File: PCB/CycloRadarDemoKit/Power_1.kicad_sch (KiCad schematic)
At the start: 33 parts, among them J701 20-16V Supply Voltage, Q701 SI2309CDS, U701 INA3221, U702 RT8259, U703 AP63205WU

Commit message: USB layout, long traces from upper prepaired
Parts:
- R710, R713: LCSC C22764 -> C22975
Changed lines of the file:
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@@
       (effects (font (size 1.27 1.27)) hide)
     )
-    (property "LCSC" "C22764" (at 212.725 127 0)
+    (property "LCSC" "C22975" (at 212.725 127 0)
       (effects (font (size 1.27 1.27)) hide)
     )
@@
       (effects (font (size 1.27 1.27)) hide)
     )
-    (property "LCSC" "C22764" (at 140.97 175.26 0)
-      (effects (font (size 1.27 1.27)) hide)
-    )
+    (property "LCSC" "C22975" (at 140.97 175.26 0)
+      (effects (font (size 1.27 1.27)) hide)
+    )

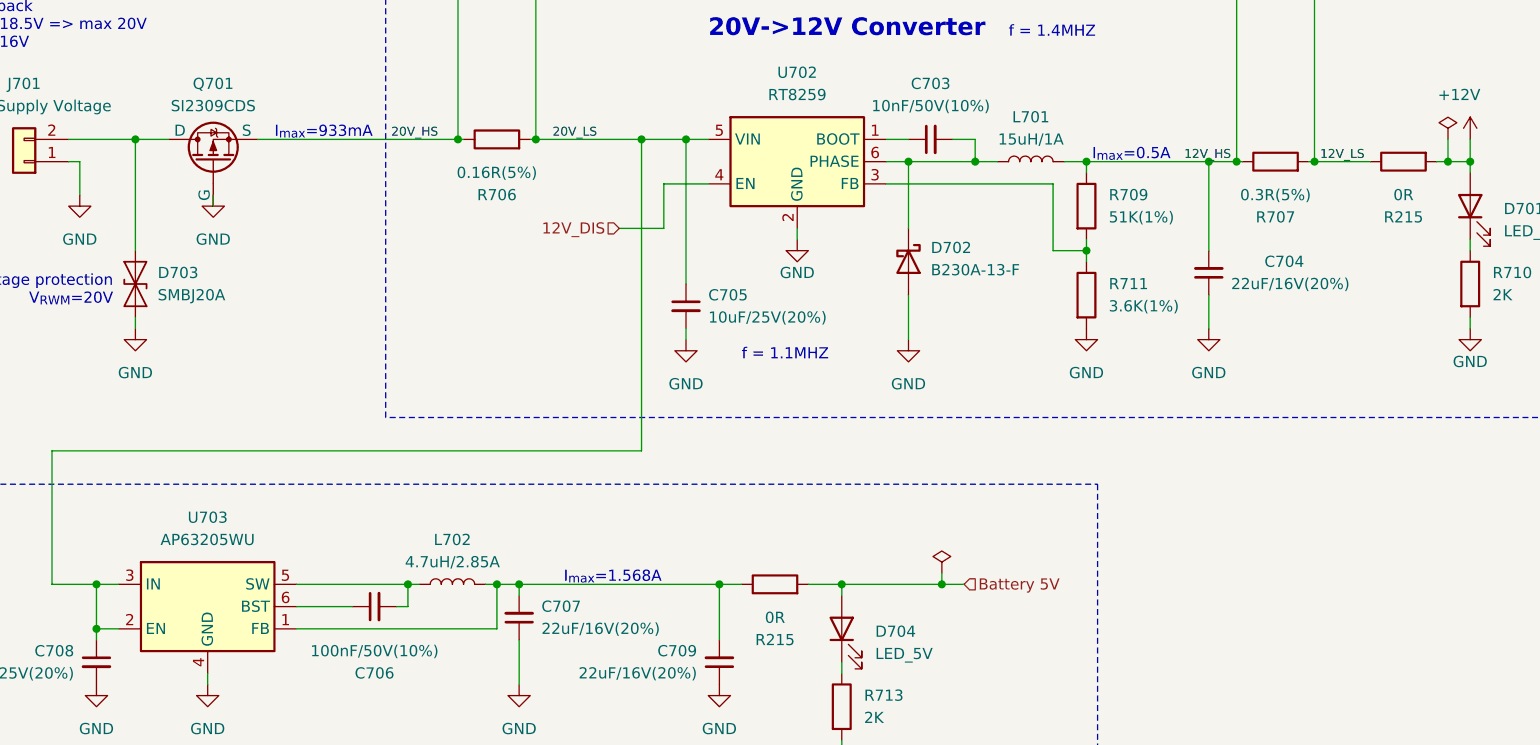
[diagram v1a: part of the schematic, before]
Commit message: DC/DC routed, stuckup properties changed
ready for PCB resize
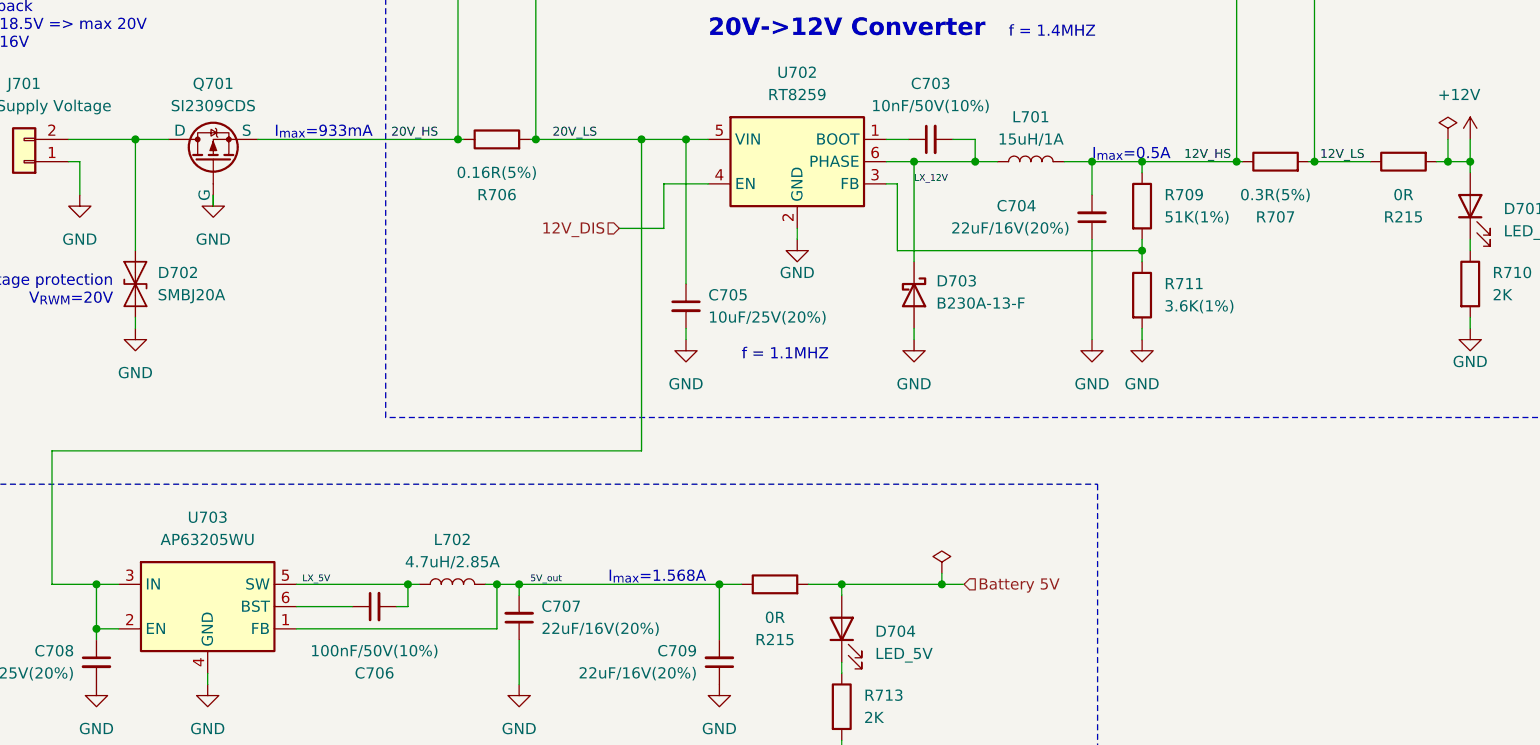
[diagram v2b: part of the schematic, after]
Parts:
- C705, C708: footprint Capacitor_SMD:C_0603_1608Metric -> Capacitor_SMD:C_1206_3216Metric; LCSC C96446 -> C13585
- renumbered D703 to D702, D702 to D703
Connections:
- net 5V_out: now reaches C707.2, C709.2, L702.2, R215.1, U703.1 (FB)
- net LX_12V: now reaches C703.2, D703.1 (K), L701.1, U702.6 (PHASE)
- net LX_5V: now reaches C706.2, L702.1, U703.5 (SW)
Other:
- moved on the sheet: C704, D703, R709, R711

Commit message: PCB routing done
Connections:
- net IN_20V: now reaches D702.2 (A2), J701.2 (Pin_2), Q701.1 (D)
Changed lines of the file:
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@@
     (effects (font (size 1.016 1.016)) (justify left bottom))
+  )
+  (label "IN_20V" (at 55.245 110.49 0) (fields_autoplaced)
+    (effects (font (size 0.762 0.762)) (justify left bottom))
   )
   (label "12V_HS" (at 185.42 113.03 180) (fields_autoplaced)

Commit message: start of repair after review
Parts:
- C705, C708: value 10uF/25V(20%) -> 10uF/50V(20%)
- R706: value 0.16R(5%) -> 0.18R(5%); footprint Resistor_SMD:R_1210_3225Metric -> Resistor_SMD:R_Shunt_LTR10EVHJLR18; LCSC C175910 -> C253348
- R707: LCSC C175910 -> C188102
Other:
- note added: "I_{max}=1.28A"
- note added: "I_{max}=842mA"
- note removed: "I_{max}=1.568A"
- note removed: "I_{max}=933mA"
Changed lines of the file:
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@@
     (effects (font (size 1.27 1.27)) (justify left bottom))
   )
-  (text "I_{max}=933mA" (at 76.2 110.49 0)
+  (text "I_{max}=842mA" (at 76.2 110.49 0)
     (effects (font (size 1.27 1.27)) (justify left bottom))
   )
@@
     (effects (font (size 1.27 1.27)) (justify left bottom))
   )
-  (text "I_{max}=1.568A" (at 114.3 161.29 0)
+  (text "I_{max}=1.28A" (at 114.3 161.29 0)
     (effects (font (size 1.27 1.27)) (justify left bottom))
   )
@@
       (effects (font (size 1.27 1.27)))
     )
-    (property "Value" "0.16R(5%)" (at 101.6 114.3 90)
-      (effects (font (size 1.27 1.27)))
-    )
-    (property "Footprint" "Resistor_SMD:R_1210_3225Metric" (at 101.6 112.268 90)
+    (property "Value" "0.18R(5%)" (at 101.6 114.3 90)
+      (effects (font (size 1.27 1.27)))
+    )
+    (property "Footprint" "Resistor_SMD:R_Shunt_LTR10EVHJLR18" (at 101.6 112.268 90)
       (effects (font (size 1.27 1.27)) hide)
     )
@@
       (effects (font (size 1.27 1.27)) hide)
     )
-    (property "LCSC" "C175910" (at 101.6 110.49 90)
+    (property "LCSC" "C253348" (at 101.6 110.49 90)
       (effects (font (size 1.27 1.27)) hide)
     )
@@
       (effects (font (size 1.27 1.27)) (justify left))
     )
-    (property "Value" "10uF/25V(20%)" (at 53.34 171.4563 0)
+    (property "Value" "10uF/50V(20%)" (at 53.34 171.4563 0)
       (effects (font (size 1.27 1.27)) (justify left))
     )
@@
       (effects (font (size 1.27 1.27)) (justify left))
     )
-    (property "Value" "10uF/25V(20%)" (at 125.73 130.8163 0)
+    (property "Value" "10uF/50V(20%)" (at 125.73 130.8163 0)
       (effects (font (size 1.27 1.27)) (justify left))
     )
@@
       (effects (font (size 1.27 1.27)) hide)
     )
-    (property "Datasheet" "~" (at 190.5 113.03 0)
+    (property "Datasheet" "https://datasheet.lcsc.com/lcsc/2304140030_TA-I-Tech-RL13FTNR300_C188102.pdf" (at 190.5 113.03 0)
       (effects (font (size 1.27 1.27)) hide)
     )
@@
       (effects (font (size 1.27 1.27)) hide)
     )
-    (property "LCSC" "C175910" (at 190.5 113.03 90)
-      (effects (font (size 1.27 1.27)) hide)
-    )
+    (property "LCSC" "C188102" (at 190.5 113.03 90)
+      (effects (font (size 1.27 1.27)) hide)
+    )

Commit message: PCB finished and reviewed
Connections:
- net 12V_HS: no longer R709.1
- net 12V_LS: now also R709.1
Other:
- moved on the sheet: C702, D701, R215, R704, R705, R707, R709, R710, R711

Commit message: JLCPCB mistakes repaired, cosmetics on PCB
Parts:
- C704, C707, C709: LCSC C87162 -> C12891
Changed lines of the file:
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@@
       (effects (font (size 1.27 1.27)) hide)
     )
-    (property "LCSC" "C87162" (at 104.14 165.1 0)
+    (property "LCSC" "C12891" (at 104.14 165.1 0)
       (effects (font (size 1.27 1.27)) hide)
     )
@@
       (effects (font (size 1.27 1.27)) hide)
     )
-    (property "LCSC" "C87162" (at 127 170.18 0)
+    (property "LCSC" "C12891" (at 127 170.18 0)
       (effects (font (size 1.27 1.27)) hide)
     )
@@
       (effects (font (size 1.27 1.27)) hide)
     )
-    (property "LCSC" "C87162" (at 169.545 119.38 0)
+    (property "LCSC" "C12891" (at 169.545 119.38 0)
       (effects (font (size 1.27 1.27)) hide)
     )

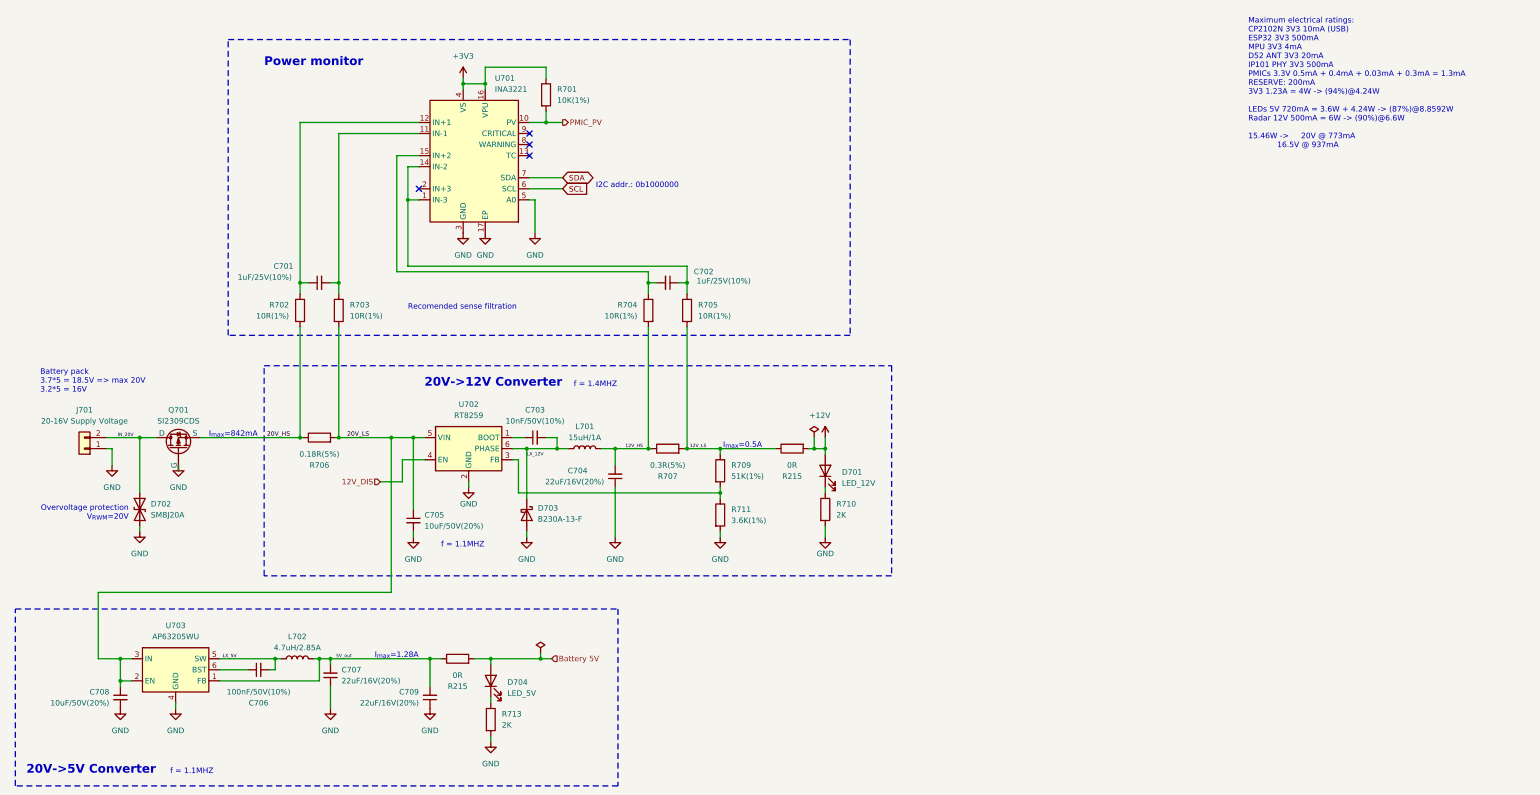
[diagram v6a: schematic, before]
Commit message: Sematic Versioning implemented, whish list added
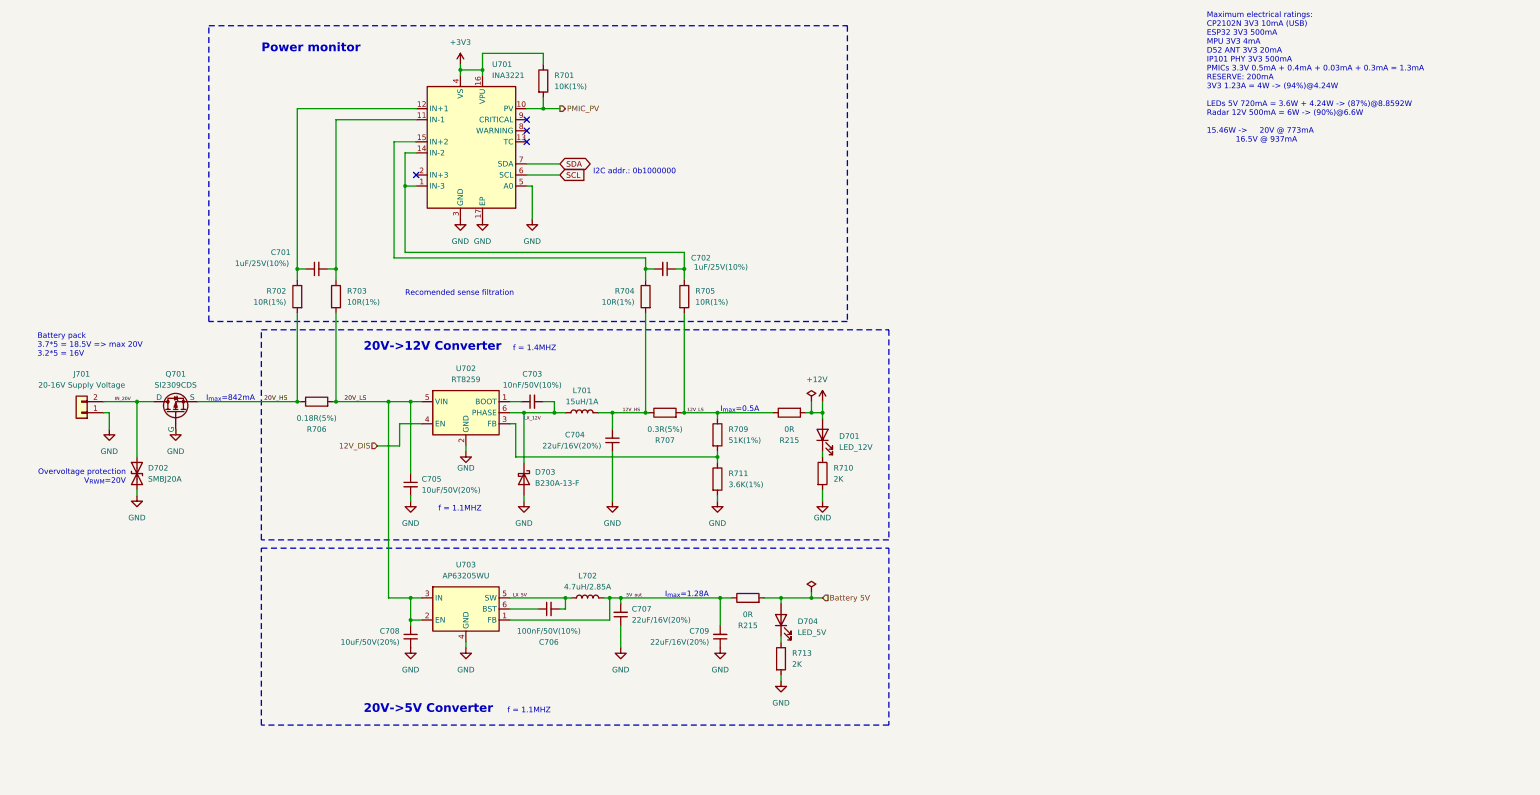
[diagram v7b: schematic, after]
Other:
- company: ALPS Electric Czech, s.r.o. -> ${COMPANY}
- title: Radar Safety Sensor -> ${TITLE}
- moved on the sheet: C701, C702, C703, C704, C705, C706, C707, C708, C709, D701, D702, D703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

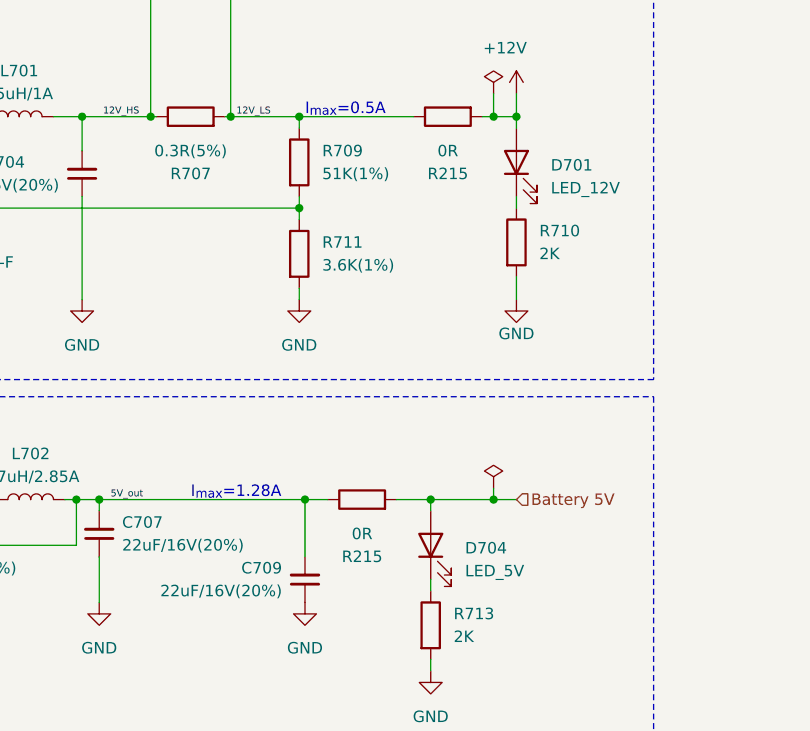
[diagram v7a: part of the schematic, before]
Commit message: photos added, readme rewrited
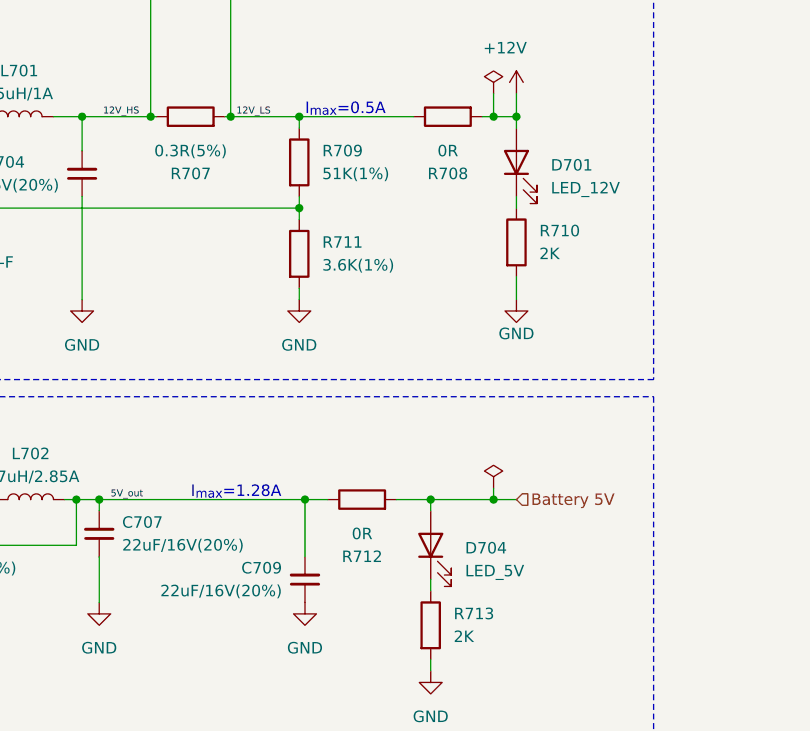
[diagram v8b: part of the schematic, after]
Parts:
- renumbered R215 to R708, R215 to R712
